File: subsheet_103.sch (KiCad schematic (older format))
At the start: 4 parts, among them J103 Cartridge Port

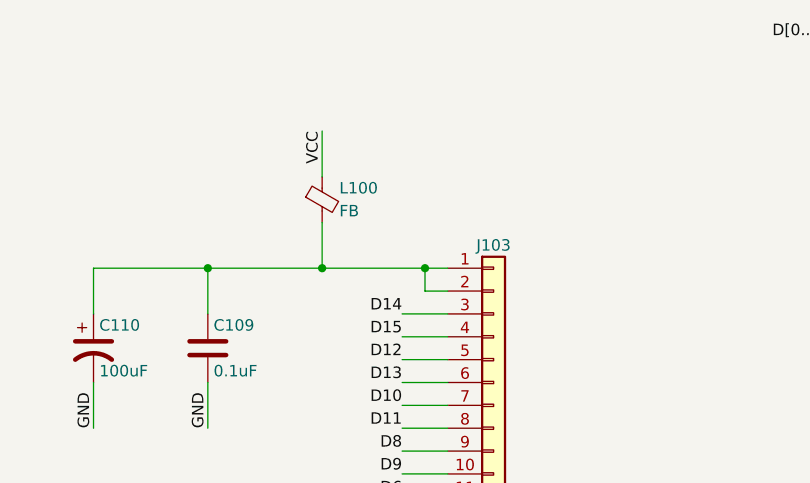
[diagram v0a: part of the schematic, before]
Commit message: Resolves #11 : Use the reference 'FB?' for the ferrite beads
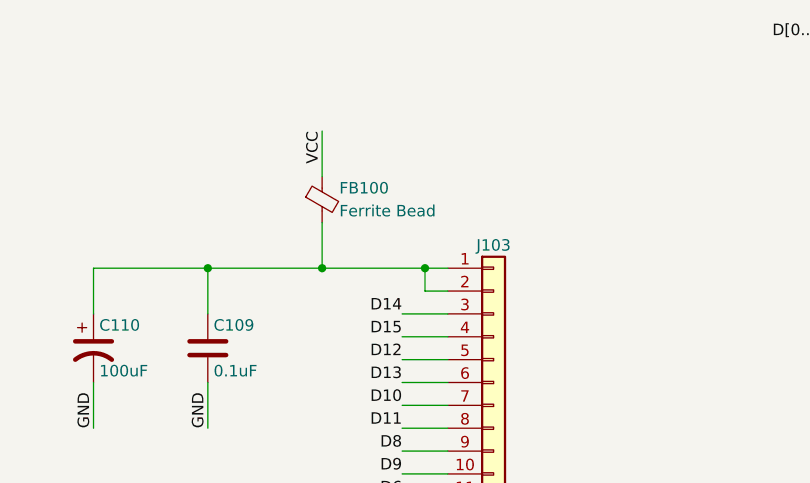
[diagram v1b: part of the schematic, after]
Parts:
- FB100: renamed from L100; value FB -> Ferrite Bead
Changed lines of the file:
@@
 	4600 5500 4800 5500
 $Comp
-L Device:Ferrite_Bead_Small L100
+L Device:Ferrite_Bead_Small FB100
 U 1 1 6085902E
 P 4250 1700
-F 0 "L100" H 4325 1750 50  0000 L CNN
-F 1 "FB" H 4325 1650 50  0000 L CNN
+F 0 "FB100" H 4325 1750 50  0000 L CNN
+F 1 "Ferrite Bead" H 4325 1650 50  0000 L CNN
 F 2 "commons_passives_THT:Passive_THT_ferrite_bead_W3.81mm_L15.24mm" V 4180 1700 50  0001 C CNN
 F 3 "~" H 4250 1700 50  0001 C CNN

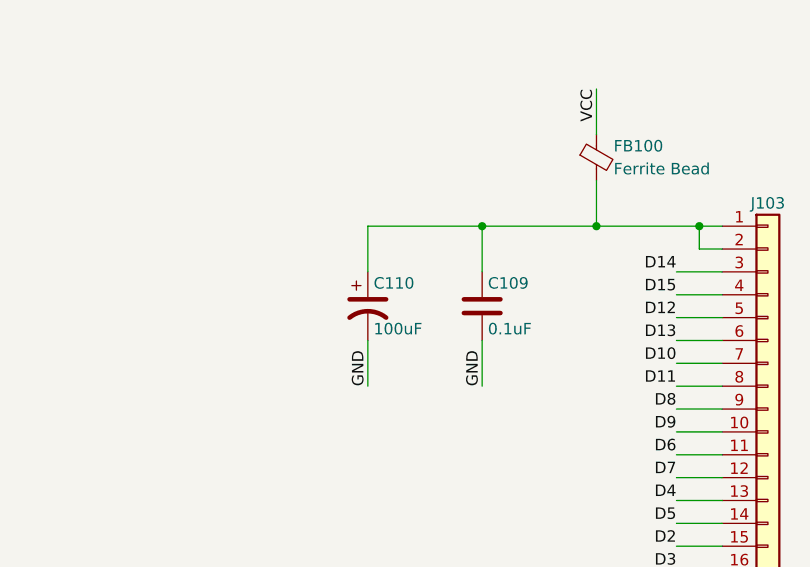
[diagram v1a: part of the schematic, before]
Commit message: Resolves #12 : Use the reference 'CP?' for polarized capacitors
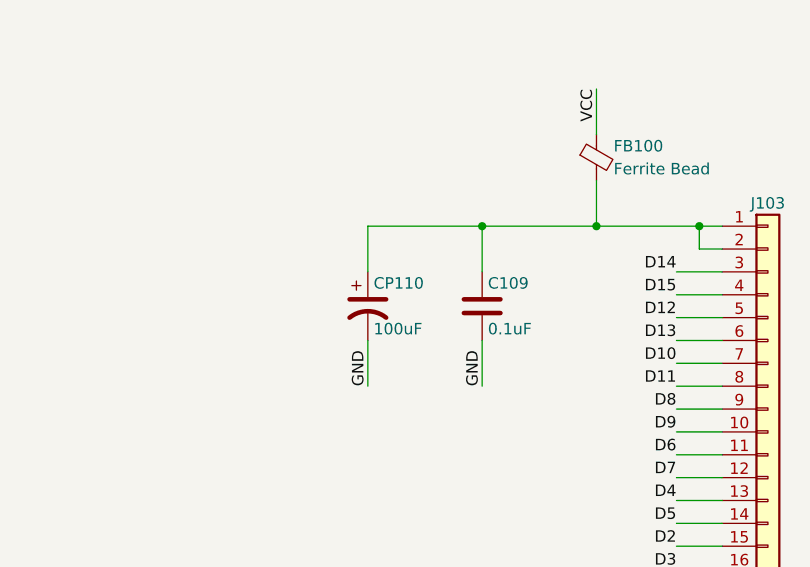
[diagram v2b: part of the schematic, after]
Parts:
- renumbered C110 to CP110
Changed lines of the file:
@@
 GND
 $Comp
-L Device:CP1 C110
+L Device:CP1 CP110
 U 1 1 6085AF1D
 P 3250 2350
-F 0 "C110" H 3275 2450 50  0000 L CNN
+F 0 "CP110" H 3275 2450 50  0000 L CNN
 F 1 "100uF" H 3275 2250 50  0000 L CNN
 F 2 "commons_passives_THT:Passive_THT_capacitor_polarized_W6.35mm_L20.32mm" H 3250 2350 50  0001 C CNN

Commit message: Resolves #8 : Assign 1206 hand-solder footprints to non polarized capacitors
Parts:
- C109: footprint commons_passives_THT:Passive_THT_capacitor_mlcc_W2.54mm_L7.62mm -> Capacitor_SMD:C_1206_3216Metric_Pad1.33x1.80mm_HandSolder
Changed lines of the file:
@@
 F 0 "C109" H 3775 2450 50  0000 L CNN
 F 1 "0.1uF" H 3775 2250 50  0000 L CNN
-F 2 "commons_passives_THT:Passive_THT_capacitor_mlcc_W2.54mm_L7.62mm" H 3788 2200 50  0001 C CNN
+F 2 "Capacitor_SMD:C_1206_3216Metric_Pad1.33x1.80mm_HandSolder" H 3788 2200 50  0001 C CNN
 F 3 "~" H 3750 2350 50  0001 C CNN
 	1    3750 2350

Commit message: Resolves #9 : Assign radial THT footprints to polarized capacitors
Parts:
- CP110: footprint commons_passives_THT:Passive_THT_capacitor_polarized_W6.35mm_L20.32mm -> Capacitor_THT:C_Radial_D8.0mm_H11.5mm_P3.50mm
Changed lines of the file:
@@
 F 0 "CP110" H 3275 2450 50  0000 L CNN
 F 1 "100uF" H 3275 2250 50  0000 L CNN
-F 2 "commons_passives_THT:Passive_THT_capacitor_polarized_W6.35mm_L20.32mm" H 3250 2350 50  0001 C CNN
+F 2 "Capacitor_THT:C_Radial_D8.0mm_H11.5mm_P3.50mm" H 3250 2350 50  0001 C CNN
 F 3 "~" H 3250 2350 50  0001 C CNN
 	1    3250 2350

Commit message: Resolves #14 : assign smd footprints for ferrite beads
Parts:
- FB100: footprint commons_passives_THT:Passive_THT_ferrite_bead_W3.81mm_L15.24mm -> Inductor_SMD:L_1206_3216Metric_Pad1.22x1.90mm_HandSolder
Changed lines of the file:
@@
 F 0 "FB100" H 4325 1750 50  0000 L CNN
 F 1 "Ferrite Bead" H 4325 1650 50  0000 L CNN
-F 2 "commons_passives_THT:Passive_THT_ferrite_bead_W3.81mm_L15.24mm" V 4180 1700 50  0001 C CNN
+F 2 "Inductor_SMD:L_1206_3216Metric_Pad1.22x1.90mm_HandSolder" V 4180 1700 50  0001 C CNN
 F 3 "~" H 4250 1700 50  0001 C CNN
 	1    4250 1700
